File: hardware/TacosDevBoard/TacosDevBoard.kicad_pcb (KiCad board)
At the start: 2 copper layers, 38.6 x 46.7 mm, 5 parts, among them J1 Conn_01x15_Socket, J2 Conn_01x15_Socket, J3 Conn_01x08_Socket, J4 Conn_01x08_Socket

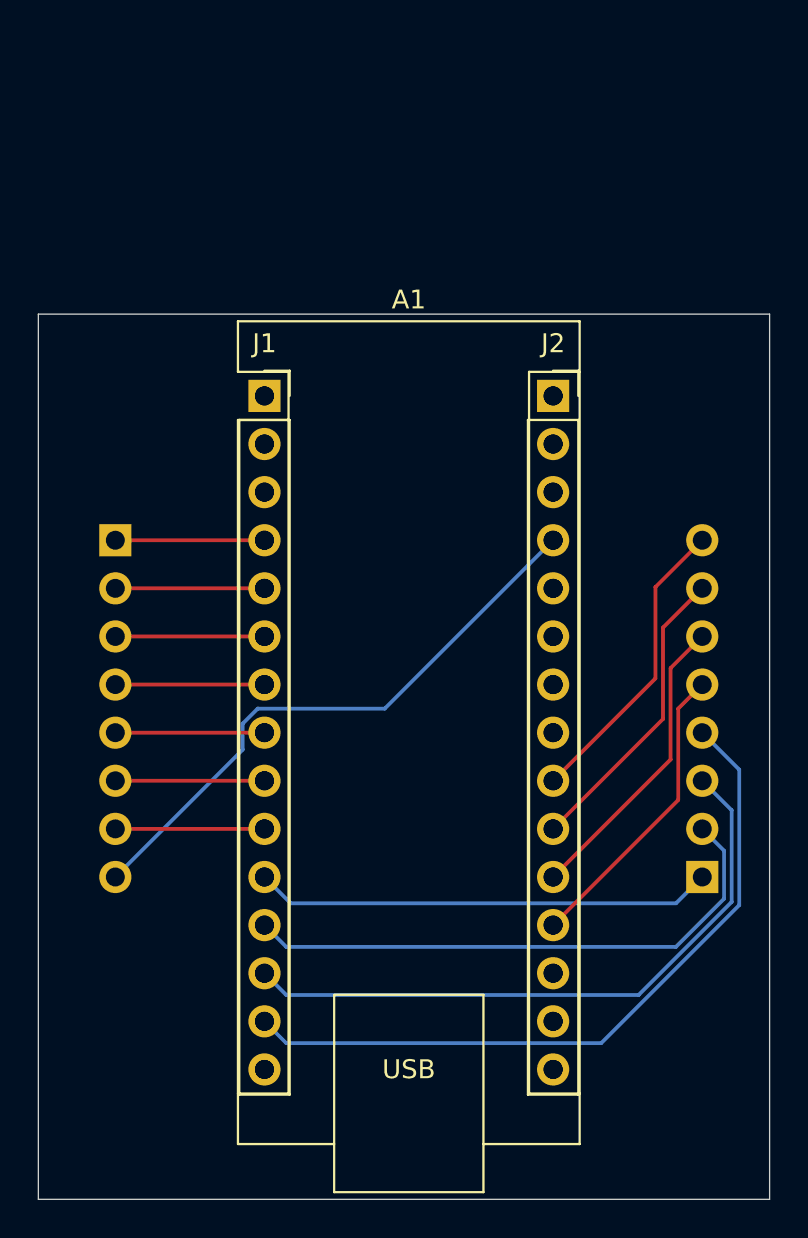
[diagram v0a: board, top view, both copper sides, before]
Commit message: Add buzzer to Dev Board
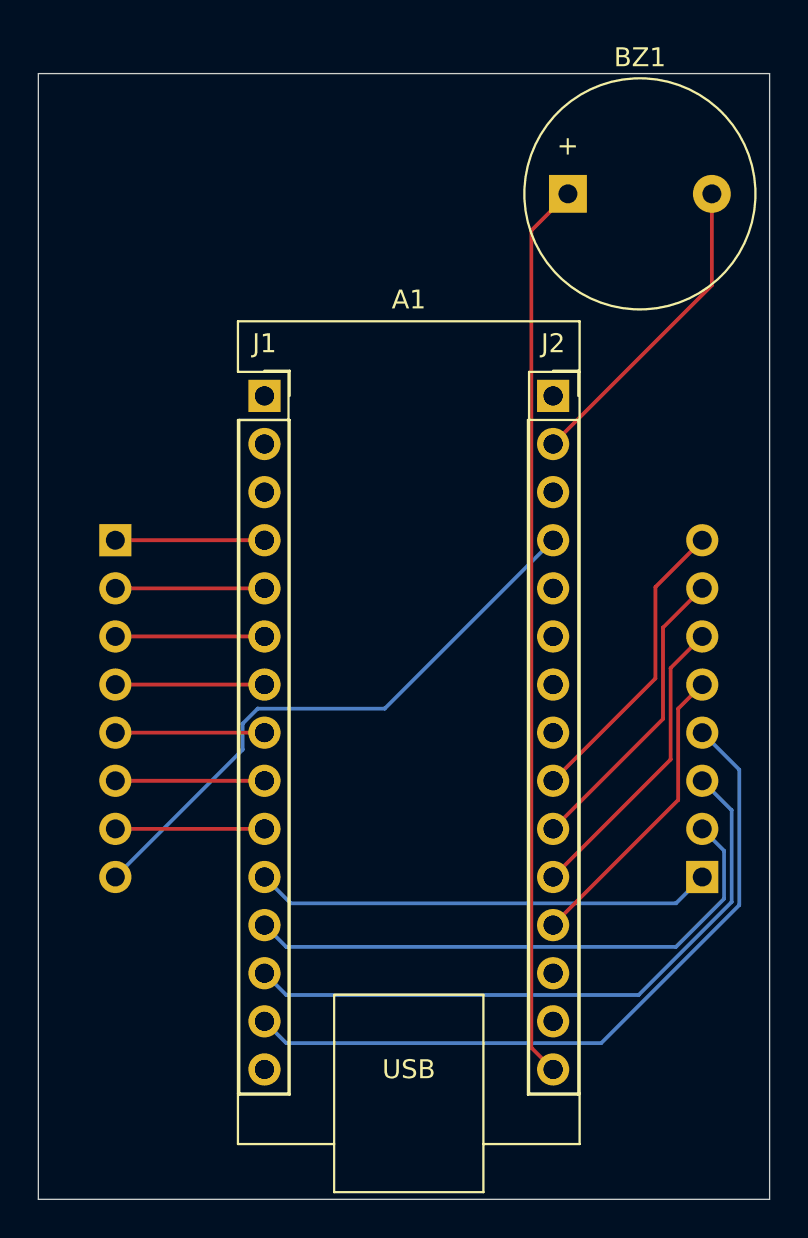
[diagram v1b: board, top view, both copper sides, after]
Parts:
- added BZ1: Buzzer, Buzzer_Beeper:Buzzer_12x9.5RM7.6, F.Cu at (139.7, 74.9)
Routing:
- net D13: track 0.00 -> 47.5 mm
- net GND: track 7.87 -> 24.6 mm
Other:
- board size 38.6 x 46.7 mm -> 38.6 x 59.4 mm
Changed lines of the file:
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@@
 		(property ki_fp_filters "Connector*:*_1x??_*")
 		(sheetname "/")
-		(sheetfile "Tacos.kicad_sch")
+		(sheetfile "TacosDevBoard.kicad_sch")
 		(attr through_hole)
 		(fp_line
@@
 		(embedded_fonts no)
 		(model "${KICAD9_3DMODEL_DIR}/Connector_PinSocket_2.54mm.3dshapes/PinSocket_1x15_P2.54mm_Vertical.step"
+			(offset
+				(xyz 0 0 0)
+			)
+			(scale
+				(xyz 1 1 1)
+			)
+			(rotate
+				(xyz 0 0 0)
+			)
+		)
+	)
+	(footprint "Buzzer_Beeper:Buzzer_12x9.5RM7.6"
+		(layer "F.Cu")
+		(at 139.72 74.93)
+		(descr "Generic Buzzer, D12mm height 9.5mm with RM7.6mm")
+		(tags "buzzer")
+		(property "Reference" "BZ1"
+			(at 3.8 -7.2 0)
+			(layer "F.SilkS")
+			(effects
+				(font
+					(size 1 1)
+					(thickness 0.15)
+				)
+			)
+		)
+		(property "Value" "Buzzer"
+			(at 3.8 7.4 0)
+			(layer "F.Fab")
+			(effects
+				(font
+					(size 1 1)
+					(thickness 0.15)
+				)
+			)
+		)
+		(property "Datasheet" "~"
+			(at 0 0 0)
+			(unlocked yes)
+			(layer "F.Fab")
+			(hide yes)
+			(effects
+				(font
+					(size 1.27 1.27)
+					(thickness 0.15)
+				)
+			)
+		)
+		(property "Description" "Buzzer, polarized"
+			(at 0 0 0)
+			(unlocked yes)
+			(layer "F.Fab")
+			(hide yes)
+			(effects
+				(font
+					(size 1.27 1.27)
+					(thickness 0.15)
+				)
+			)
+		)
+		(property ki_fp_filters "*Buzzer*")
+		(sheetname "/")
+		(sheetfile "TacosDevBoard.kicad_sch")
+		(attr through_hole)
+		(fp_circle
+			(center 3.8 0)
+			(end 9.9 0)
+			(stroke
+				(width 0.12)
+				(type solid)
+			)
+			(fill no)
+			(layer "F.SilkS")
+		)
+		(fp_circle
+			(center 3.8 0)
+			(end 10.05 0)
+			(stroke
+				(width 0.05)
+				(type solid)
+			)
+			(fill no)
+			(layer "F.CrtYd")
+		)
+		(fp_circle
+			(center 3.8 0)
+			(end 4.8 0)
+			(stroke
+				(width 0.1)
+				(type solid)
+			)
+			(fill no)
+			(layer "F.Fab")
+		)
+		(fp_circle
+			(center 3.8 0)
+			(end 9.8 0)
+			(stroke
+				(width 0.1)
+				(type solid)
+			)
+			(fill no)
+			(layer "F.Fab")
+		)
+		(fp_text user "+"
+			(at -0.01 -2.54 0)
+			(layer "F.SilkS")
+			(effects
+				(font
+					(size 1 1)
+					(thickness 0.15)
+				)
+			)
+		)
+		(fp_text user "+"
+			(at -0.01 -2.54 0)
+			(layer "F.Fab")
+			(effects
+				(font
+					(size 1 1)
+					(thickness 0.15)
+				)
+			)
+		)
+		(fp_text user "${REFERENCE}"
+			(at 3.8 -4 0)
+			(layer "F.Fab")
+			(effects
+				(font
+					(size 1 1)
+					(thickness 0.15)
+				)
+			)
+		)
+		(pad "1" thru_hole rect
+			(at 0 0)
+			(size 2 2)
+			(drill 1)
+			(layers "*.Cu" "*.Mask")
+			(remove_unused_layers no)
+			(net 19 "D13")
+			(pinfunction "+")
+			(pintype "passive")
+		)
+		(pad "2" thru_hole circle
+			(at 7.6 0)
+			(size 2 2)
+			(drill 1)
+			(layers "*.Cu" "*.Mask")
+			(remove_unused_layers no)
+			(net 23 "GND")
+			(pinfunction "-")
+			(pintype "passive")
+		)
+		(embedded_fonts no)
+		(model "${KICAD9_3DMODEL_DIR}/Buzzer_Beeper.3dshapes/Buzzer_12x9.5RM7.6.step"
 			(offset
 				(xyz 0 0 0)
@@
 		(property ki_fp_filters "Arduino*Nano*")
 		(sheetname "/")
-		(sheetfile "Tacos.kicad_sch")
+		(sheetfile "TacosDevBoard.kicad_sch")
 		(attr through_hole exclude_from_pos_files)
 		(fp_line
@@
 		(property ki_fp_filters "Connector*:*_1x??_*")
 		(sheetname "/")
-		(sheetfile "Tacos.kicad_sch")
+		(sheetfile "TacosDevBoard.kicad_sch")
 		(attr through_hole)
 		(fp_line
@@
 		(property ki_fp_filters "Connector*:*_1x??_*")
 		(sheetname "/")
-		(sheetfile "Tacos.kicad_sch")
+		(sheetfile "TacosDevBoard.kicad_sch")
 		(attr through_hole)
 		(fp_line
@@
 		(property ki_fp_filters "Connector*:*_1x??_*")
 		(sheetname "/")
-		(sheetfile "Tacos.kicad_sch")
+		(sheetfile "TacosDevBoard.kicad_sch")
 		(attr through_hole)
 		(fp_line
@@
 	)
 	(gr_rect
-		(start 111.76 81.28)
+		(start 111.76 68.58)
 		(end 150.368 128.016)
 		(stroke
@@
 	)
 	(segment
+		(start 137.787 120.007)
+		(end 137.787 76.863)
+		(width 0.2)
+		(layer "F.Cu")
+		(net 19)
+	)
+	(segment
+		(start 138.938 121.158)
+		(end 137.787 120.007)
+		(width 0.2)
+		(layer "F.Cu")
+		(net 19)
+	)
+	(segment
+		(start 137.787 76.863)
+		(end 139.72 74.93)
+		(width 0.2)
+		(layer "F.Cu")
+		(net 19)
+	)
+	(segment
 		(start 145.141 99.969)
 		(end 145.141 104.795)
@@
 		(width 0.2)
 		(layer "F.Cu")
+		(net 23)
+	)
+	(segment
+		(start 147.32 79.756)
+		(end 138.938 88.138)
+		(width 0.2)
+		(layer "F.Cu")
+		(net 23)
+	)
+	(segment
+		(start 147.32 74.93)
+		(end 147.32 79.756)
+		(width 0.2)
+		(layer "F.Cu")

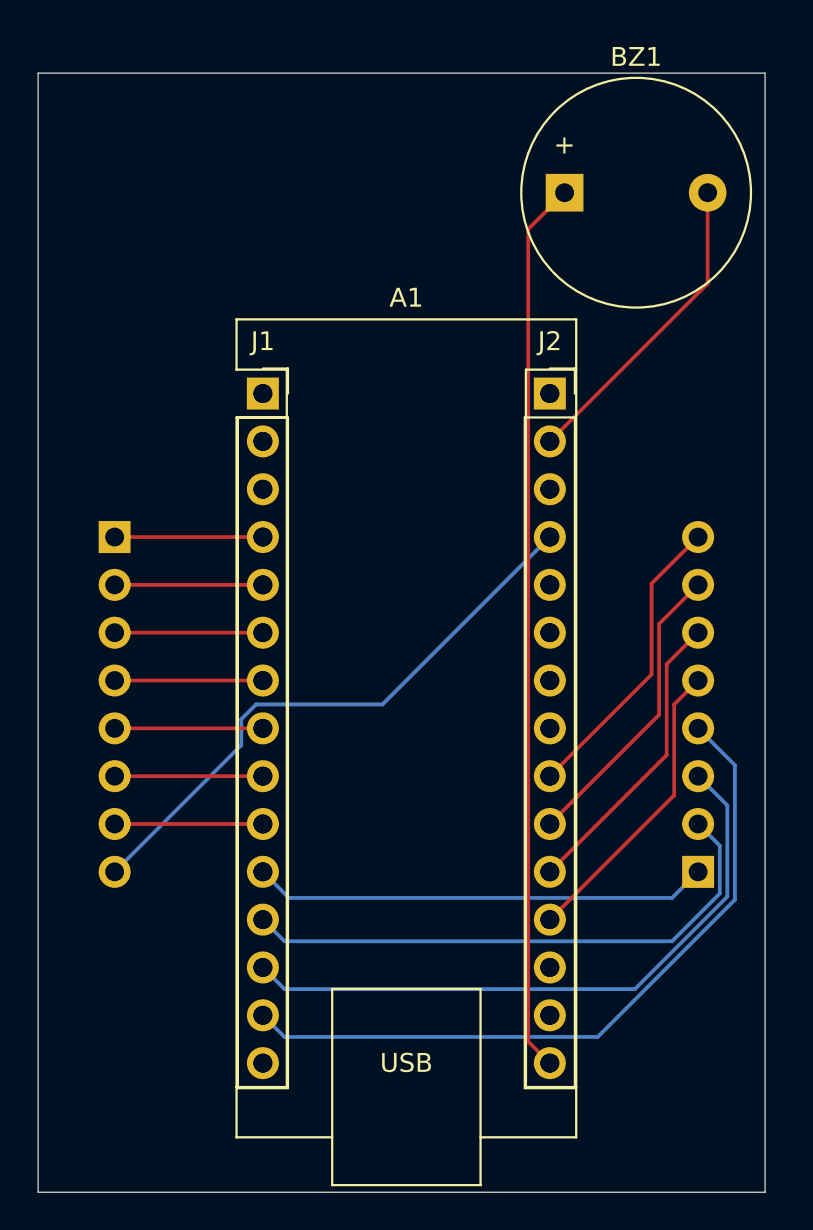
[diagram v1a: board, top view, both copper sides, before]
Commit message: Add orthogonal dimensions to dev board
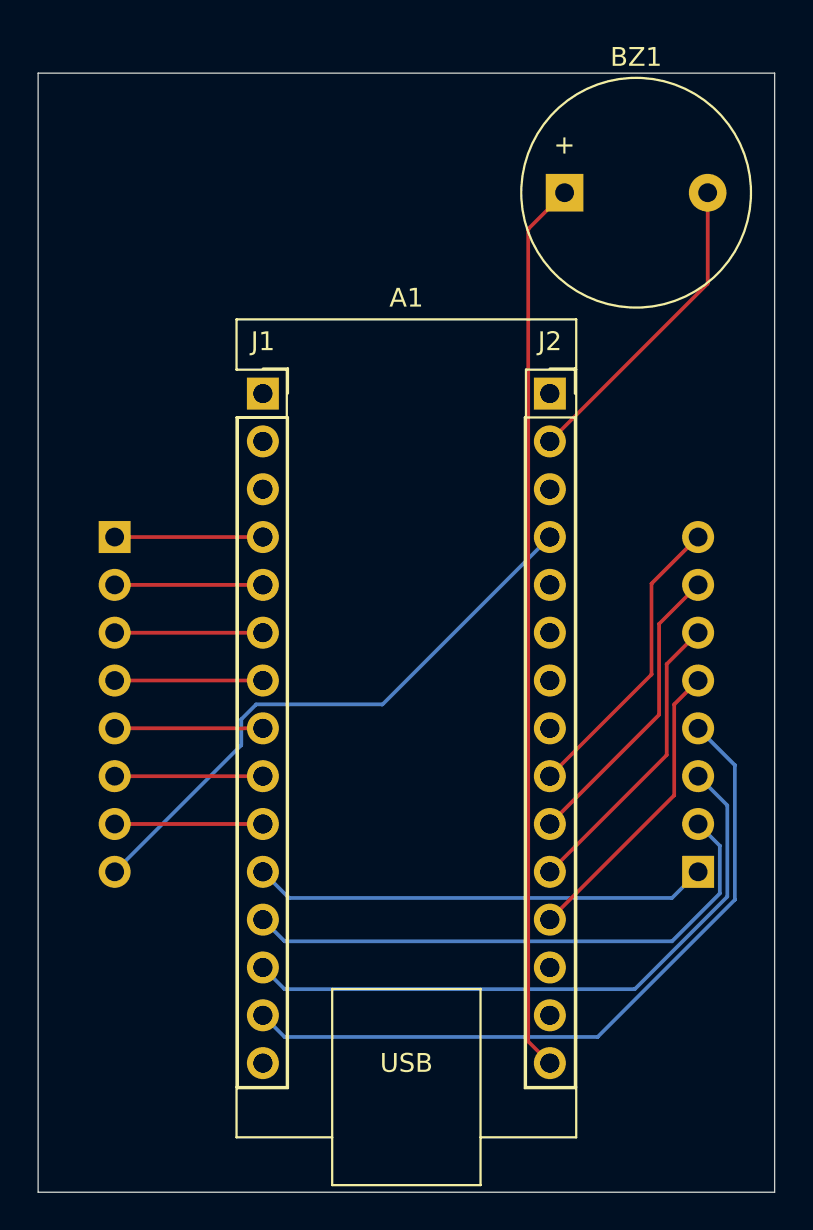
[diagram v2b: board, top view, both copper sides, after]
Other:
- board size 38.6 x 59.4 mm -> 39.1 x 59.4 mm
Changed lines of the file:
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@@
 	(gr_rect
 		(start 111.76 68.58)
-		(end 150.368 128.016)
+		(end 150.876 128.016)
 		(stroke
 			(width 0.05)
@@
 		(layer "Edge.Cuts")
 	)
+	(dimension
+		(type orthogonal)
+		(layer "Cmts.User")
+		(pts
+			(xy 150.876 68.58) (xy 111.76 68.58)
+		)
+		(height -2.54)
+		(orientation 0)
+		(format
+			(prefix "")
+			(suffix "in")
+			(units 0)
+			(units_format 0)
+			(precision 4)
+			(suppress_zeroes yes)
+		)
+		(style
+			(thickness 0.2)
+			(arrow_length 1.27)
+			(text_position_mode 0)
+			(arrow_direction outward)
+			(extension_height 0.58642)
+			(extension_offset 0.5)
+			(keep_text_aligned yes)
+		)
+		(gr_text "1.54in"
+			(at 131.318 64.24 0)
+			(layer "Cmts.User")
+			(effects
+				(font
+					(size 1.5 1.5)
+					(thickness 0.3)
+				)
+			)
+		)
+	)
+	(dimension
+		(type orthogonal)
+		(layer "Cmts.User")
+		(pts
+			(xy 146.812 93.218) (xy 115.824 93.218)
+		)
+		(height -11.938)
+		(orientation 0)
+		(format
+			(prefix "")
+			(suffix "in")
+			(units 0)
+			(units_format 0)
+			(precision 4)
+			(suppress_zeroes yes)
+		)
+		(style
+			(thickness 0.2)
+			(arrow_length 1.27)
+			(text_position_mode 0)
+			(arrow_direction outward)
+			(extension_height 0.58642)
+			(extension_offset 0.5)
+			(keep_text_aligned yes)
+		)
+		(gr_text "1.22in"
+			(at 131.318 79.48 0)
+			(layer "Cmts.User")
+			(effects
+				(font
+					(size 1.5 1.5)
+					(thickness 0.3)
+				)
+			)
+		)
+	)
+	(dimension
+		(type orthogonal)
+		(layer "Cmts.User")
+		(pts
+			(xy 138.938 85.598) (xy 123.698 85.598)
+		)
+		(height 0)
+		(orientation 0)
+		(format
+			(prefix "")
+			(suffix "in")
+			(units 0)
+			(units_format 0)
+			(precision 4)
+			(suppress_zeroes yes)
+		)
+		(style
+			(thickness 0.2)
+			(arrow_length 1.27)
+			(text_position_mode 0)
+			(arrow_direction outward)
+			(extension_height 0.58642)
+			(extension_offset 0.5)
+			(keep_text_aligned yes)
+		)
+		(gr_text "0.6in"
+			(at 131.318 83.798 0)
+			(layer "Cmts.User")
+			(effects
+				(font
+					(size 1.5 1.5)
+					(thickness 0.3)
+				)
+			)
+		)
+	)
 	(segment

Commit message: finished mega pcb
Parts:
- removed A1: Arduino_Nano_v3.x, Module:Arduino_Nano
- added IC2_COMM1: Conn_01x08_Socket, Connector_PinSocket_2.54mm:PinSocket_1x08_P2.54mm_Vertical, B.Cu at (152.9, 38.1)
- added J3: Conn_01x08_Socket, Connector_PinHeader_2.54mm:PinHeader_1x08_P2.54mm_Vertical, F.Cu at (161.1, 70.9)
- added J4: Conn_01x08_Socket, Connector_PinHeader_2.54mm:PinHeader_1x08_P2.54mm_Vertical, F.Cu at (113.0, 111.4)
- added J5: Conn_01x08_Socket, Connector_PinHeader_2.54mm:PinHeader_1x08_P2.54mm_Vertical, F.Cu at (113.0, 88.5)
- added J7: Conn_02x17_Counter_Clockwise, Connector_PinHeader_2.54mm:PinHeader_2x17_P2.54mm_Vertical, F.Cu at (153.7, 136.9)
- added J9: Conn_01x10_Pin, Connector_PinHeader_2.54mm:PinHeader_1x10_P2.54mm_Vertical, F.Cu at (112.9, 61.4)
- J1, J2: value Conn_01x15_Socket -> Conn_01x08_Socket; footprint Connector_PinSocket_2.54mm:PinSocket_1x15_P2.54mm_Vertical -> Connector_PinHeader_2.54mm:PinHeader_1x08_P2.54mm_Vertical
- moved PWM1 61.2 mm to (120.1, 55.9)
- moved J1 48.5 mm to (161.1, 116.4)
- moved SELECT1 40.0 mm to (127.5, 131.5), turned to -90 degrees
- moved BZ1 35.6 mm to (161.6, 46.8)
- moved J2 23.6 mm to (161.1, 93.6)
- renumbered J4 to PWM1, J3 to SELECT1
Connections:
- J1 pad 1: TX1 -> unconnected-(J1-Pin_1-Pad1)
- J1 pad 2: RX0 -> unconnected-(J1-Pin_2-Pad2)
- J1 pad 3: RST -> unconnected-(J1-Pin_3-Pad3)
- J1 pad 4: GND -> unconnected-(J1-Pin_4-Pad4)
- J1 pad 5: D2 -> unconnected-(J1-Pin_5-Pad5)
- J1 pad 6: D3 -> unconnected-(J1-Pin_6-Pad6)
- J1 pad 7: D4 -> unconnected-(J1-Pin_7-Pad7)
- J1 pad 8: D5 -> unconnected-(J1-Pin_8-Pad8)
- J2 pad 1: VIN -> unconnected-(J2-Pin_1-Pad1)
- J2 pad 2: GND -> unconnected-(J2-Pin_2-Pad2)
- J2 pad 3: RST -> unconnected-(J2-Pin_3-Pad3)
- J2 pad 4: +5V -> unconnected-(J2-Pin_4-Pad4)
- J2 pad 5: A7 -> unconnected-(J2-Pin_5-Pad5)
- J2 pad 6: A6 -> unconnected-(J2-Pin_6-Pad6)
- J2 pad 7: A5 -> unconnected-(J2-Pin_7-Pad7)
- J2 pad 8: A4 -> unconnected-(J2-Pin_8-Pad8)
- PWM1 pad 1: D8 -> ~D2
- PWM1 pad 2: D9 -> ~D3
- PWM1 pad 3: D10 -> ~D4
- PWM1 pad 4: D11 -> ~D5
- PWM1 pad 5: A0 -> ~D6
- PWM1 pad 6: A1 -> ~D7
- PWM1 pad 7: A2 -> ~D8
- PWM1 pad 8: A3 -> ~D9
- SELECT1 pad 2: D2 -> D22
- SELECT1 pad 3: D3 -> D24
- SELECT1 pad 4: D4 -> D26
- SELECT1 pad 5: D5 -> D28
- SELECT1 pad 6: D6 -> D30
- SELECT1 pad 7: D7 -> D32
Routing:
- net RX1: track 0.00 -> 118.5 mm
- net GND: track 24.6 -> 139.3 mm
- net TX0: track 0.00 -> 101.0 mm
- net RX0: track 0.00 -> 97.6 mm
- net RX2: track 0.00 -> 96.2 mm
- net TX3: track 0.00 -> 93.3 mm
- net TX1: track 0.00 -> 92.4 mm
- net TX2: track 0.00 -> 92.4 mm
- net RX3: track 0.00 -> 87.3 mm
- net ~D7: track 0.00 -> 68.3 mm
- net ~D6: track 0.00 -> 62.9 mm
- net ~D5: track 0.00 -> 57.5 mm
- net ~D4: track 0.00 -> 52.1 mm
- net D13: track 47.5 -> 0.00 mm
- net ~D3: track 0.00 -> 46.6 mm
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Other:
- board size 39.1 x 59.4 mm -> 63.6 x 108.1 mm
- board text added: "${REFERENCE}"

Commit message: finished dev board
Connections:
- BZ1 pad 1: D13 -> D52
- J3 pad 4: unconnected-(J3-Pin_4-Pad4) -> +3.3V
- J3 pad 5: unconnected-(J3-Pin_5-Pad5) -> +5V
- J3 pad 6: unconnected-(J3-Pin_6-Pad6) -> GND
- J3 pad 7: unconnected-(J3-Pin_7-Pad7) -> GND
- J3 pad 8: unconnected-(J3-Pin_8-Pad8) -> VIN
- J7 pad 17: unconnected-(J7-Pin_17-Pad17) -> D52
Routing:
- net D52: track 0.00 -> 117.0 mm
- net +5V: track 0.00 -> 57.0 mm
- net GND: track 139.3 -> 161.2 mm

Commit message: started adding SD card
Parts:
- added J6: Micro_SD_Card_Det2, Connector_Card:microSD_HC_Molex_104031-0811, B.Cu at (165.0, 44.0)
- moved BZ1 13.7 mm to (161.4, 60.5)
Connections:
- J7 pad 18: unconnected-(J7-Pin_18-Pad18) -> Net-(J6-VSS)
- J7 pad 26: unconnected-(J7-Pin_26-Pad26) -> Net-(J6-DET_B)
- J7 pad 27: unconnected-(J7-Pin_27-Pad27) -> Net-(J6-DET_A)
- J7 pad 28: unconnected-(J7-Pin_28-Pad28) -> Net-(J6-DAT1)
- J7 pad 29: unconnected-(J7-Pin_29-Pad29) -> Net-(J6-DAT0)
- J7 pad 30: unconnected-(J7-Pin_30-Pad30) -> Net-(J6-CLK)
- J7 pad 31: unconnected-(J7-Pin_31-Pad31) -> Net-(J6-CMD)
- J7 pad 32: unconnected-(J7-Pin_32-Pad32) -> Net-(J6-DAT3/CD)
- J7 pad 33: unconnected-(J7-Pin_33-Pad33) -> Net-(J6-DAT2)
- J7 pad 34: unconnected-(J7-Pin_34-Pad34) -> Net-(J6-VDD)
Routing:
- net GND: track 161.2 -> 26.4 mm
- net D52: track 117.0 -> 90.3 mm
